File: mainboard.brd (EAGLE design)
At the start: 90.2 x 95.9 mm, 69 parts, among them J1 POWER_JACKPTH_LOCK, T1 SINGLE_NCHAN_FET, T2 MOSFET_PCHAN_20A, T3 SINGLE_NCHAN_FET, T4 MOSFET_PCHAN_20A, T5 SINGLE_NCHAN_FET, T6 MOSFET_PCHAN_20A, T7 MOSFET_PCHAN_20A, T8 SINGLE_NCHAN_FET, U1 MURATA_REG_OKL-T3-W12, U2 TEENSY_3.0+4, U3 RFM23BP, U4 HMC5883LSMD, U5 ITG-3200, U7 CURRENT_MAX4372, U8 CURRENT_MAX4372

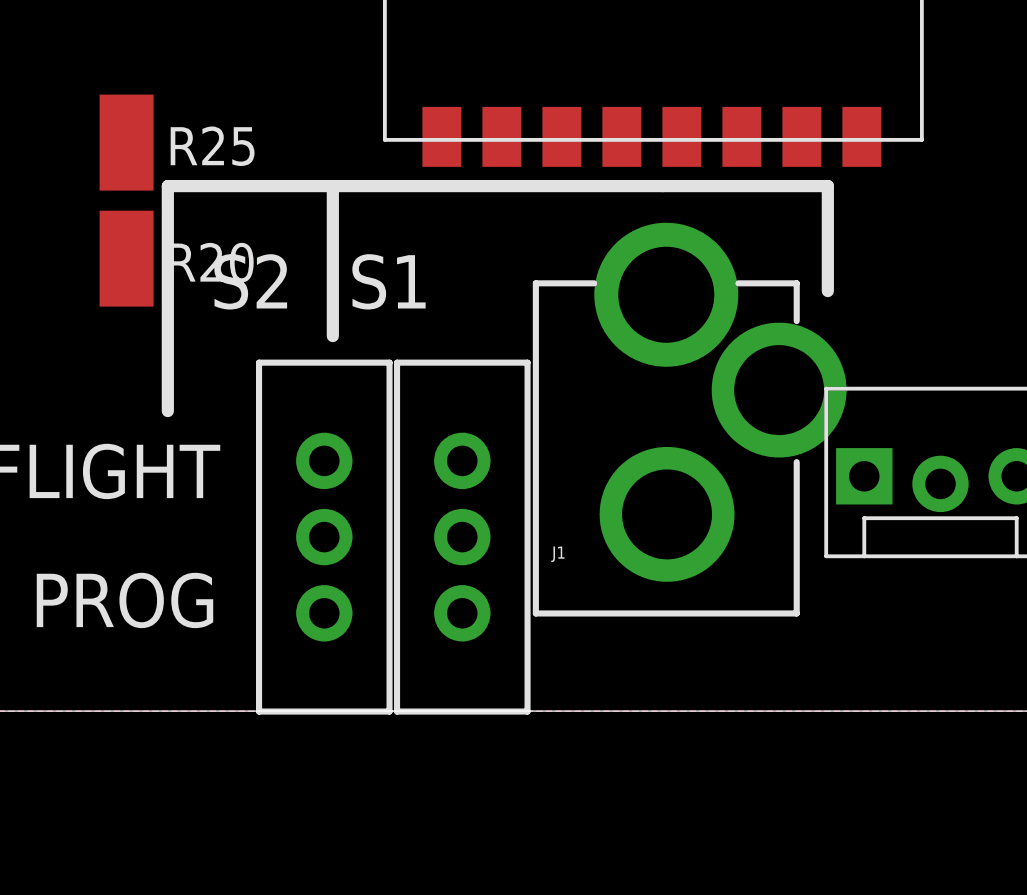
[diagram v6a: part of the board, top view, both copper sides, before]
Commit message: Moved power connector
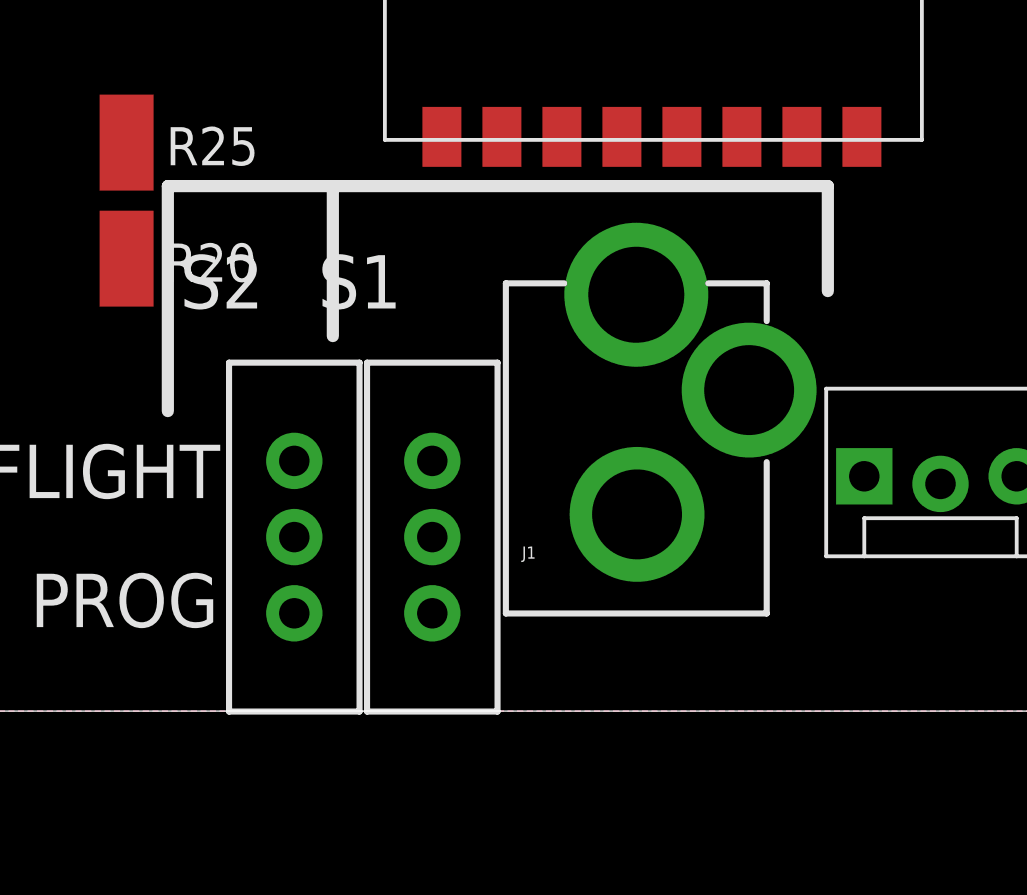
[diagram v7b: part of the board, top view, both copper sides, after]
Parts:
- moved J1 1.00 mm to (49.7, 0.00)
- moved S1 1.00 mm to (42.9, 5.80)
- moved S2 1.00 mm to (38.3, 5.80)
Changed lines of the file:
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@@
 <wire x1="34.085" y1="10" x2="34.085" y2="17.5" width="0.4064" layer="21"/>
 <wire x1="34.085" y1="17.5" x2="39.585" y2="17.5" width="0.4064" layer="21"/>
-<wire x1="39.585" y1="17.5" x2="50.585" y2="17.5" width="0.4064" layer="21"/>
-<wire x1="50.585" y1="17.5" x2="56.085" y2="17.5" width="0.4064" layer="21"/>
+<wire x1="39.585" y1="17.5" x2="56.085" y2="17.5" width="0.4064" layer="21"/>
 <wire x1="56.085" y1="17.5" x2="56.085" y2="14" width="0.4064" layer="21"/>
 <wire x1="34.085" y1="95.885" x2="34.085" y2="78.385" width="0.4064" layer="21"/>
@@
 <element name="R12" library="SparkFun-Resistors" package="0805" value="10K" x="-57" y="-62.4"/>
 <element name="R13" library="SparkFun-Resistors" package="0805" value="4.7K" x="-54" y="-62.4"/>
-<element name="J1" library="SparkFun-Connectors" package="POWER_JACK_PTH_LOCK" value="POWER_JACKPTH_LOCK" x="50.7" y="0">
-<attribute name="PROD_ID" value="PRT-00119" x="50.7" y="0" size="1.778" layer="27" display="off"/>
+<element name="J1" library="SparkFun-Connectors" package="POWER_JACK_PTH_LOCK" value="POWER_JACKPTH_LOCK" x="49.7" y="0">
+<attribute name="PROD_ID" value="PRT-00119" x="49.7" y="0" size="1.778" layer="27" display="off"/>
 </element>
 <element name="U$3" library="SparkFun-Boards" package="ARDUINO_PRO_MINI" value="ARDUINO_PRO_MINI" x="74" y="25" rot="R180"/>
 <element name="R14" library="SparkFun-Resistors" package="0805" value="10k" x="-95.9" y="-62.4"/>
-<element name="S1" library="SparkFun-Electromechanical" package="SWITCH-SPDT" value="" x="43.9" y="5.8"/>
-<element name="S2" library="SparkFun-Electromechanical" package="SWITCH-SPDT" value="" x="39.3" y="5.8"/>
+<element name="S1" library="SparkFun-Electromechanical" package="SWITCH-SPDT" value="" x="42.9" y="5.8"/>
+<element name="S2" library="SparkFun-Electromechanical" package="SWITCH-SPDT" value="" x="38.3" y="5.8"/>
 </elements>
 <signals>
@@
 <wire x1="11.51" y1="51.53" x2="16.9" y2="41.027" width="0" layer="19" extent="1-1"/>
 <wire x1="8.99" y1="51.64" x2="11.51" y2="51.53" width="0" layer="19" extent="1-1"/>
-<wire x1="45.22" y1="19.14" x2="54.4616" y2="10.7" width="0" layer="19" extent="1-1"/>
+<wire x1="45.22" y1="19.14" x2="53.4616" y2="10.7" width="0" layer="19" extent="1-1"/>
 <wire x1="57.22" y1="51.94" x2="69.4" y2="45.127" width="0" layer="19" extent="1-1"/>
 </signal>
@@
 <contactref element="ST1" pad="1"/>
 <contactref element="J1" pad="PWR"/>
-<wire x1="19.23" y1="13.9322" x2="50.7" y2="13.8778" width="0" layer="19" extent="1-1"/>
+<wire x1="19.23" y1="13.9322" x2="49.7" y2="13.8778" width="0" layer="19" extent="1-1"/>
 <wire x1="12.09" y1="17.7878" x2="19.23" y2="13.9322" width="0" layer="19" extent="1-1"/>
 <wire x1="12.09" y1="24.7878" x2="12.09" y2="17.7878" width="0" layer="19" extent="1-1"/>
@@
 <contactref element="U$3" pad="21"/>
 <contactref element="S2" pad="3"/>
-<wire x1="39.3" y1="3.26" x2="66.38" y2="19.92" width="0" layer="19" extent="1-1"/>
+<wire x1="38.3" y1="3.26" x2="66.38" y2="19.92" width="0" layer="19" extent="1-1"/>
 </signal>
 <signal name="N$11">
 <contactref element="U2" pad="23/A9"/>
 <contactref element="S1" pad="2"/>
-<wire x1="43.9" y1="5.8" x2="52.705" y2="85.89" width="0" layer="19" extent="1-1"/>
+<wire x1="42.9" y1="5.8" x2="52.705" y2="85.89" width="0" layer="19" extent="1-1"/>
 </signal>
 <signal name="PGM_RST">
 <contactref element="U$3" pad="22"/>
 <contactref element="S1" pad="3"/>
-<wire x1="43.9" y1="3.26" x2="66.38" y2="17.38" width="0" layer="19" extent="1-1"/>
+<wire x1="42.9" y1="3.26" x2="66.38" y2="17.38" width="0" layer="19" extent="1-1"/>
 </signal>
 <signal name="N$13">
 <contactref element="S2" pad="2"/>
 <contactref element="U2" pad="VUSB"/>
-<wire x1="39.3" y1="5.8" x2="50.165" y2="90.97" width="0" layer="19" extent="1-1"/>
+<wire x1="38.3" y1="5.8" x2="50.165" y2="90.97" width="0" layer="19" extent="1-1"/>
 </signal>
 </signals>

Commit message: Fixed charging jack on schematic
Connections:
- net GND: no longer J1.GND, J1.GNDBREAK
- net N$1: now also J1.GND, J1.GNDBREAK
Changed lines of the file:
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@@
 <contactref element="R13" pad="1"/>
 <via x="5.09" y="5.08" extent="1-16" drill="3.175" diameter="5"/>
-<contactref element="J1" pad="GNDBREAK"/>
-<contactref element="J1" pad="GND"/>
 <contactref element="U$3" pad="23"/>
 <contactref element="U$3" pad="4"/>
 <contactref element="R14" pad="1"/>
-<wire x1="-56.05" y1="-60.2" x2="-96.8" y2="-62.4" width="0" layer="19" extent="1-1"/>
-<wire x1="-54.9" y1="-62.4" x2="-56.05" y2="-60.2" width="0" layer="19" extent="1-1"/>
-<wire x1="-49.4" y1="-57.4" x2="-56.05" y2="-60.2" width="0" layer="19" extent="1-1"/>
-<wire x1="-52.3" y1="1.8" x2="-49.4" y2="-57.4" width="0" layer="19" extent="1-1"/>
-<wire x1="-55.1" y1="1.8" x2="-52.3" y2="1.8" width="0" layer="19" extent="1-1"/>
-<wire x1="-57.9" y1="1.8" x2="-55.1" y2="1.8" width="0" layer="19" extent="1-1"/>
-<wire x1="5.09" y1="5.08" x2="-52.3" y2="1.8" width="0" layer="19" extent="1-1"/>
-<wire x1="28.98" y1="30.4901" x2="33.1701" y2="31.7501" width="0" layer="19" extent="1-1"/>
-<wire x1="25.47" y1="32.29" x2="28.98" y2="30.4901" width="0" layer="19" extent="1-1"/>
-<wire x1="10.1" y1="72" x2="5.627" y2="68.6" width="0" layer="19" extent="1-1"/>
-<wire x1="21.01" y1="28.61" x2="25.47" y2="32.29" width="0" layer="19" extent="1-1"/>
-<wire x1="17.05" y1="32.6301" x2="21.01" y2="28.61" width="0" layer="19" extent="1-1"/>
-<wire x1="13.35" y1="34.3" x2="17.05" y2="32.6301" width="0" layer="19" extent="1-1"/>
-<wire x1="30.4" y1="85.5" x2="32.8" y2="91.873" width="0" layer="19" extent="1-1"/>
-<wire x1="12.485" y1="79.5" x2="10.1" y2="72" width="0" layer="19" extent="1-1"/>
-<wire x1="18.2" y1="69.2" x2="10.1" y2="72" width="0" layer="19" extent="1-1"/>
-<wire x1="21.7" y1="67.7" x2="18.2" y2="69.2" width="0" layer="19" extent="1-1"/>
-<wire x1="43.22" y1="51.94" x2="45.085" y2="60.49" width="0" layer="19" extent="1-1"/>
-<wire x1="77.62" y1="57.41" x2="85.873" y2="62.6" width="0" layer="19" extent="1-1"/>
-<wire x1="77.53" y1="54.8" x2="77.62" y2="57.41" width="0" layer="19" extent="1-1"/>
-<wire x1="23.661" y1="78.357" x2="30.4" y2="85.5" width="0" layer="19" extent="1-1"/>
-<wire x1="61.31" y1="84.21" x2="52.705" y2="90.97" width="0" layer="19" extent="1-1"/>
-<wire x1="63.09" y1="83.51" x2="61.31" y2="84.21" width="0" layer="19" extent="1-1"/>
+<wire x1="69.08" y1="88.09" x2="82.55" y2="90.805" width="0" layer="19" extent="1-1"/>
+<wire x1="65.34" y1="86.76" x2="69.08" y2="88.09" width="0" layer="19" extent="1-1"/>
+<wire x1="64.34" y1="86.76" x2="65.34" y2="86.76" width="0" layer="19" extent="1-1"/>
+<wire x1="63.09" y1="83.51" x2="64.34" y2="86.76" width="0" layer="19" extent="1-1"/>
+<wire x1="61.31" y1="84.21" x2="63.09" y2="83.51" width="0" layer="19" extent="1-1"/>
 <wire x1="62.54" y1="81.45" x2="63.09" y2="83.51" width="0" layer="19" extent="1-1"/>
-<wire x1="64.34" y1="86.76" x2="63.09" y2="83.51" width="0" layer="19" extent="1-1"/>
-<wire x1="65.34" y1="86.76" x2="64.34" y2="86.76" width="0" layer="19" extent="1-1"/>
 <wire x1="67.09" y1="83.51" x2="65.34" y2="86.76" width="0" layer="19" extent="1-1"/>
-<wire x1="64.83" y1="90.6" x2="64.34" y2="86.76" width="0" layer="19" extent="1-1"/>
-<wire x1="69.08" y1="88.09" x2="65.34" y2="86.76" width="0" layer="19" extent="1-1"/>
+<wire x1="64.83" y1="90.6" x2="65.34" y2="86.76" width="0" layer="19" extent="1-1"/>
 <wire x1="61.19" y1="76.11" x2="62.54" y2="81.45" width="0" layer="19" extent="1-1"/>
 <wire x1="62.49" y1="74.43" x2="61.19" y2="76.11" width="0" layer="19" extent="1-1"/>
 <wire x1="63.49" y1="74.43" x2="62.49" y2="74.43" width="0" layer="19" extent="1-1"/>
 <wire x1="63" y1="68.67" x2="62.49" y2="74.43" width="0" layer="19" extent="1-1"/>
+<wire x1="52.705" y1="90.97" x2="61.31" y2="84.21" width="0" layer="19" extent="1-1"/>
+<wire x1="37.465" y1="93.51" x2="52.705" y2="90.97" width="0" layer="19" extent="1-1"/>
+<wire x1="32.8" y1="91.873" x2="37.465" y2="93.51" width="0" layer="19" extent="1-1"/>
+<wire x1="30.4" y1="85.5" x2="32.8" y2="91.873" width="0" layer="19" extent="1-1"/>
+<wire x1="23.661" y1="78.357" x2="30.4" y2="85.5" width="0" layer="19" extent="1-1"/>
+<wire x1="18.2" y1="69.2" x2="23.661" y2="78.357" width="0" layer="19" extent="1-1"/>
+<wire x1="21.7" y1="67.7" x2="18.2" y2="69.2" width="0" layer="19" extent="1-1"/>
+<wire x1="10.1" y1="72" x2="18.2" y2="69.2" width="0" layer="19" extent="1-1"/>
+<wire x1="5.627" y1="68.6" x2="10.1" y2="72" width="0" layer="19" extent="1-1"/>
+<wire x1="12.485" y1="79.5" x2="10.1" y2="72" width="0" layer="19" extent="1-1"/>
 <wire x1="24.67" y1="56.67" x2="21.7" y2="67.7" width="0" layer="19" extent="1-1"/>
 <wire x1="24.57" y1="54.16" x2="24.67" y2="56.67" width="0" layer="19" extent="1-1"/>
-<wire x1="11.51" y1="51.53" x2="16.9" y2="41.027" width="0" layer="19" extent="1-1"/>
+<wire x1="8.89" y1="90.805" x2="12.485" y2="79.5" width="0" layer="19" extent="1-1"/>
+<wire x1="11.51" y1="51.53" x2="24.57" y2="54.16" width="0" layer="19" extent="1-1"/>
 <wire x1="8.99" y1="51.64" x2="11.51" y2="51.53" width="0" layer="19" extent="1-1"/>
-<wire x1="45.22" y1="19.14" x2="53.4616" y2="10.7" width="0" layer="19" extent="1-1"/>
-<wire x1="57.22" y1="51.94" x2="69.4" y2="45.127" width="0" layer="19" extent="1-1"/>
+<wire x1="16.9" y1="41.027" x2="11.51" y2="51.53" width="0" layer="19" extent="1-1"/>
+<wire x1="13.35" y1="34.3" x2="16.9" y2="41.027" width="0" layer="19" extent="1-1"/>
+<wire x1="17.05" y1="32.6301" x2="13.35" y2="34.3" width="0" layer="19" extent="1-1"/>
+<wire x1="21.01" y1="28.61" x2="17.05" y2="32.6301" width="0" layer="19" extent="1-1"/>
+<wire x1="25.47" y1="32.29" x2="21.01" y2="28.61" width="0" layer="19" extent="1-1"/>
+<wire x1="28.98" y1="30.4901" x2="25.47" y2="32.29" width="0" layer="19" extent="1-1"/>
+<wire x1="33.1701" y1="31.7501" x2="28.98" y2="30.4901" width="0" layer="19" extent="1-1"/>
+<wire x1="38.2699" y1="31.7501" x2="33.1701" y2="31.7501" width="0" layer="19" extent="1-1"/>
+<wire x1="38.2699" y1="36.8499" x2="38.2699" y2="31.7501" width="0" layer="19" extent="1-1"/>
+<wire x1="33.1701" y1="36.8499" x2="33.1701" y2="31.7501" width="0" layer="19" extent="1-1"/>
+<wire x1="45.22" y1="19.14" x2="38.2699" y2="31.7501" width="0" layer="19" extent="1-1"/>
+<wire x1="43.22" y1="51.94" x2="38.2699" y2="36.8499" width="0" layer="19" extent="1-1"/>
+<wire x1="45.085" y1="60.49" x2="43.22" y2="51.94" width="0" layer="19" extent="1-1"/>
+<wire x1="57.22" y1="51.94" x2="43.22" y2="51.94" width="0" layer="19" extent="1-1"/>
+<wire x1="69.4" y1="45.127" x2="57.22" y2="51.94" width="0" layer="19" extent="1-1"/>
+<wire x1="77.53" y1="54.8" x2="69.4" y2="45.127" width="0" layer="19" extent="1-1"/>
+<wire x1="77.62" y1="57.41" x2="77.53" y2="54.8" width="0" layer="19" extent="1-1"/>
+<wire x1="85.873" y1="62.6" x2="77.62" y2="57.41" width="0" layer="19" extent="1-1"/>
+<wire x1="57.3" y1="7.827" x2="45.22" y2="19.14" width="0" layer="19" extent="1-1"/>
+<wire x1="66.38" y1="14.84" x2="57.3" y2="7.827" width="0" layer="19" extent="1-1"/>
+<wire x1="81.62" y1="19.92" x2="66.38" y2="14.84" width="0" layer="19" extent="1-1"/>
+<wire x1="85.09" y1="5.08" x2="81.62" y2="19.92" width="0" layer="19" extent="1-1"/>
+<wire x1="16.4778" y1="8" x2="21.01" y2="28.61" width="0" layer="19" extent="1-1"/>
+<wire x1="5.09" y1="5.08" x2="16.4778" y2="8" width="0" layer="19" extent="1-1"/>
+<wire x1="-52.3" y1="1.8" x2="5.09" y2="5.08" width="0" layer="19" extent="1-1"/>
+<wire x1="-55.1" y1="1.8" x2="-52.3" y2="1.8" width="0" layer="19" extent="1-1"/>
+<wire x1="-57.9" y1="1.8" x2="-55.1" y2="1.8" width="0" layer="19" extent="1-1"/>
+<wire x1="-49.4" y1="-57.4" x2="-52.3" y2="1.8" width="0" layer="19" extent="1-1"/>
+<wire x1="-56.05" y1="-60.2" x2="-49.4" y2="-57.4" width="0" layer="19" extent="1-1"/>
+<wire x1="-54.9" y1="-62.4" x2="-56.05" y2="-60.2" width="0" layer="19" extent="1-1"/>
+<wire x1="-96.8" y1="-62.4" x2="-56.05" y2="-60.2" width="0" layer="19" extent="1-1"/>
 </signal>
 <signal name="VREG_IN">
@@
 <contactref element="ST2" pad="2"/>
 <contactref element="ST1" pad="2"/>
-<wire x1="12.09" y1="13.9322" x2="12.09" y2="20.9322" width="0" layer="19" extent="1-1"/>
-<wire x1="12.6222" y1="8" x2="12.09" y2="13.9322" width="0" layer="19" extent="1-1"/>
+<contactref element="J1" pad="GNDBREAK"/>
+<contactref element="J1" pad="GND"/>
+<wire x1="49.7254" y1="6.557" x2="53.4616" y2="10.7" width="0" layer="19" extent="1-1"/>
+<wire x1="12.6222" y1="8" x2="49.7254" y2="6.557" width="0" layer="19" extent="1-1"/>
+<wire x1="12.09" y1="13.9322" x2="12.6222" y2="8" width="0" layer="19" extent="1-1"/>
+<wire x1="12.09" y1="20.9322" x2="12.09" y2="13.9322" width="0" layer="19" extent="1-1"/>
 </signal>
 <signal name="N$8">
